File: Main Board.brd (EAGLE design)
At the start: 82.5 x 69.8 mm, 19 parts, among them U1 TPS61030RSAR

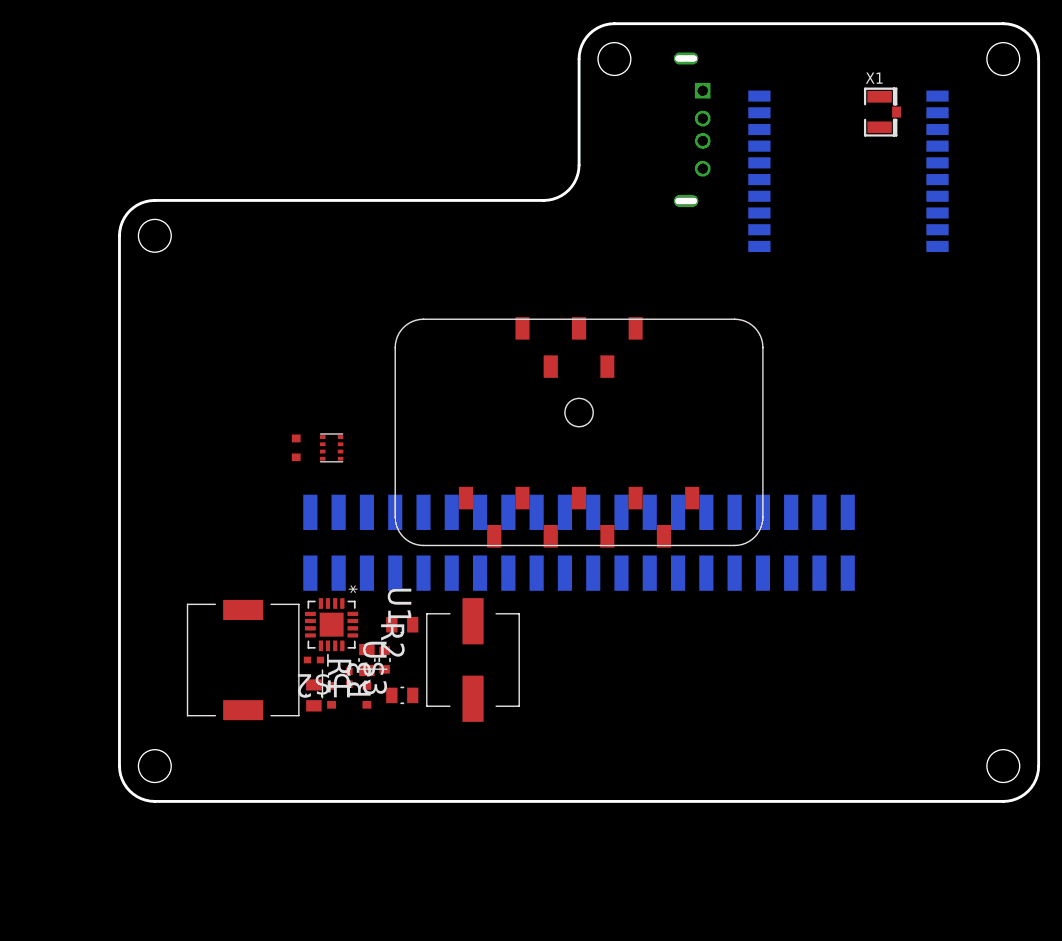
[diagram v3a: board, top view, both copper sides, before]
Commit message: Completed Motor Driver schematic
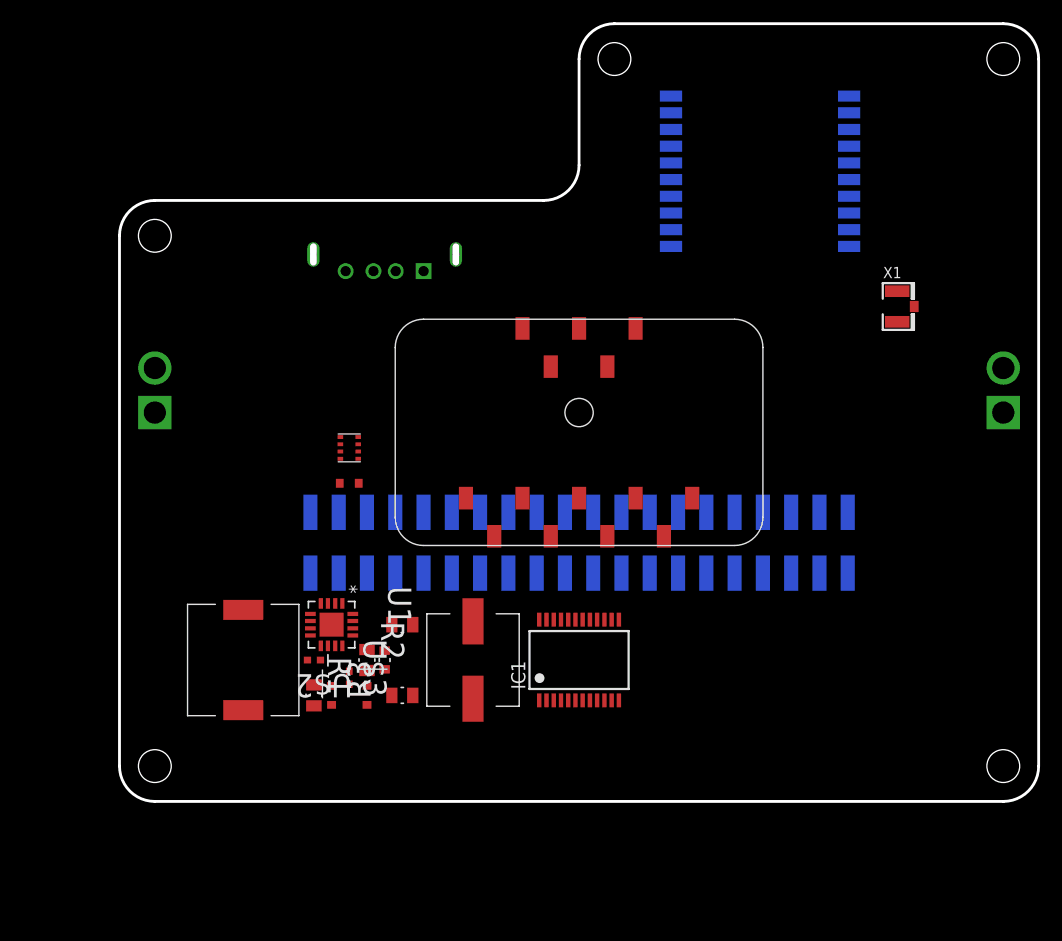
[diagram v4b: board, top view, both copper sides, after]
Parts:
- added IC1: TB6612FNG, Adafruit:SSOP24
- added U$15, U$16: MOTOR2, GoatFinder:BAT
- moved U$8 31.3 mm to (-17.5, 12.7), turned to 0 degrees
- moved X1 17.5 mm to (28.6, 9.53)
- moved U$5 7.94 mm to (15.9, 17.5)
- moved U$14 5.72 mm to (-20.6, -6.35), turned to 180 degrees
- moved U$13 1.59 mm to (-20.6, -3.17), turned to 0 degrees
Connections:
- new net +12V: IC1.13, IC1.14, IC1.24
- new net N$15: IC1.22, U$11.GPIO2
- new net N$16: IC1.1, IC1.2, U$15.P$1
- new net N$17: IC1.5, IC1.6, U$15.P$2
- new net N$18: IC1.7, IC1.8, U$16.P$1
- new net N$19: IC1.11, IC1.12, U$16.P$2
- new net N$20: IC1.21, U$11.GPIO3
- new net N$21: IC1.19, U$11.GPIO4
- new net N$22: IC1.17, U$11.GPIO5
- new net N$23: IC1.16, U$11.GPIO6
- new net PWMA: IC1.23, U$11.GPIO23
- new net PWMB: IC1.15, U$11.GPIO26
- net +3.3V: now also IC1.20
- net GND: now also IC1.10, IC1.18, IC1.3, IC1.4, IC1.9
- net N$10: now also U$11.SCL1; no longer U$11.SCL0
- net N$12: now also U$11.SDA1; no longer U$11.SDA0
- net N$13: now also U$11.SDA0; no longer U$11.SDA1
- net N$14: now also U$11.SCL0; no longer U$11.SCL1

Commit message: Modified part placment
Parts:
- moved U$3 29.5 mm to (-38.1, 0.00)
- moved R3 29.3 mm to (-36.5, 0.00)
- moved U$4 29.3 mm to (-38.1, -3.17)
- moved U$9 29.3 mm to (-34.9, -3.17)
- moved R1 29.2 mm to (-34.9, 1.59)
- moved R2 29.1 mm to (-33.3, 3.17)
- moved U$7 28.6 mm to (-31.8, 1.59)
- moved U$1 27.2 mm to (-33.3, 4.76), turned to 180 degrees
- moved U$12 26.3 mm to (-33.3, -11.1), turned to 180 degrees
- moved U$10 24.7 mm to (-33.3, -1.59)
- moved U$2 24.2 mm to (-33.3, 0.00)
- moved IC1 22.1 mm to (7.94, -1.59), flipped to the bottom, turned to 270 degrees
- moved U$5 19.4 mm to (0.00, 6.35)
- moved U$15 17.5 mm to (-20.6, 0.00), turned to 270 degrees
- moved U$16 17.5 mm to (20.6, 0.00), turned to 270 degrees
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
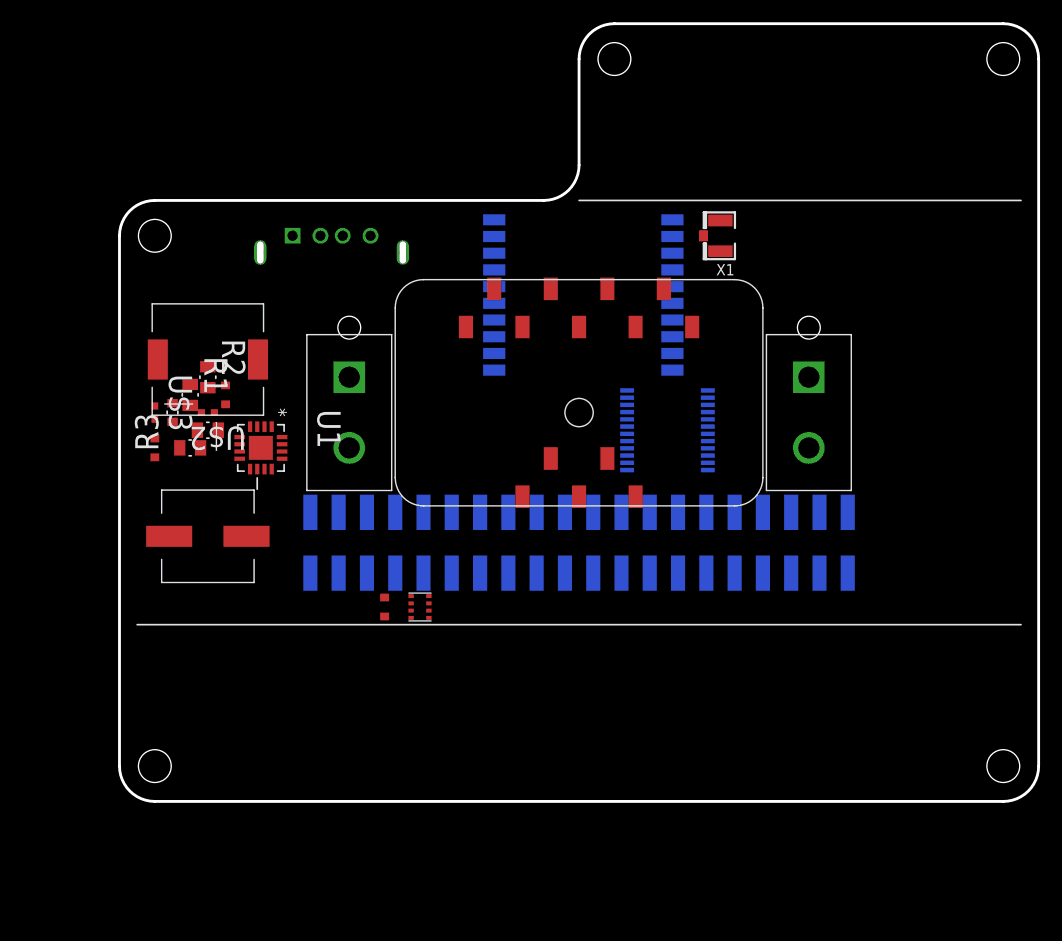
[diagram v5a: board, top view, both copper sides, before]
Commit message: Reduced Board Size and added Ground Planes
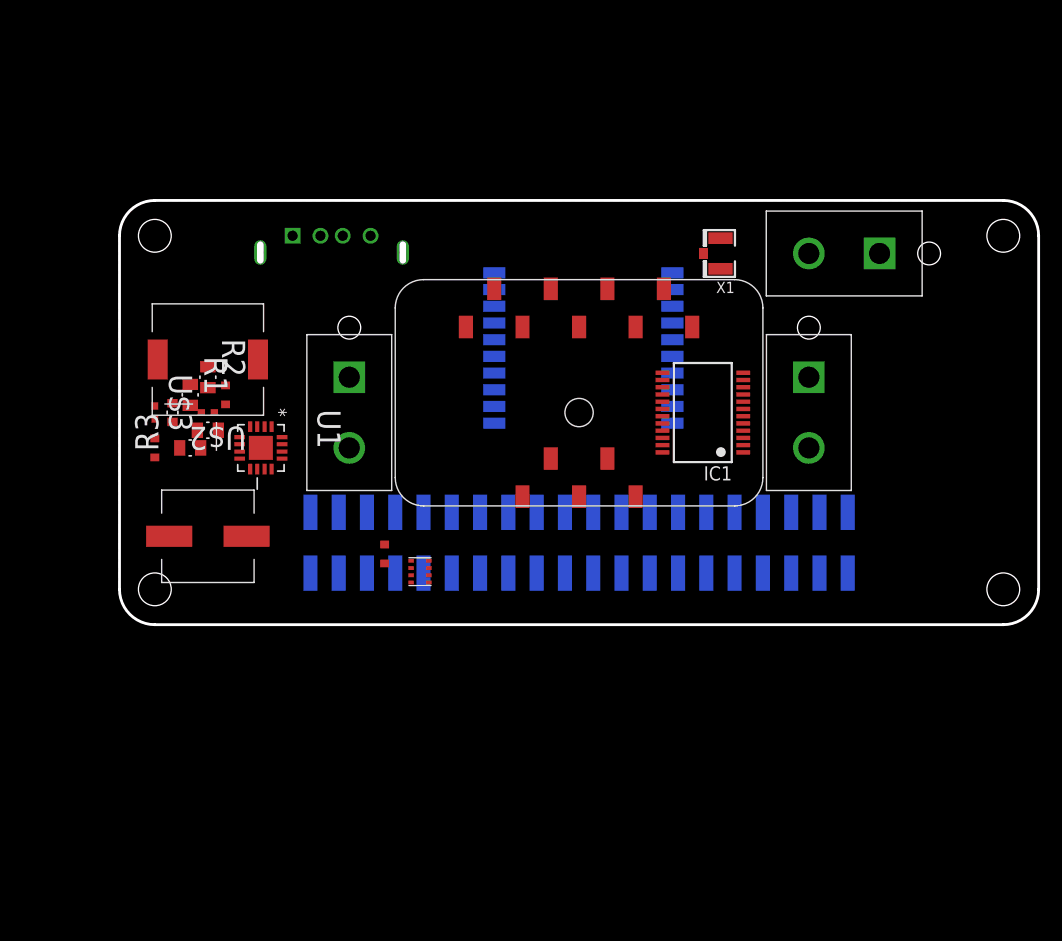
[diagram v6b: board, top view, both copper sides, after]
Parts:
- added U$17: MOTOR2, GoatFinder:BAT
- moved U$14 4.76 mm to (-17.5, -12.7)
- moved U$5 4.76 mm to (0.00, 1.59)
- moved IC1 3.55 mm to (11.1, 0.00), flipped to the top, turned to 90 degrees
- moved U$13 3.17 mm to (-14.3, -14.3)
- moved X1 1.59 mm to (12.7, 14.3)
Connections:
- removed net +12V: IC1.13, IC1.14, IC1.24
- net GND: now also U$17.P$2
- net VBAT: now also IC1.13, IC1.14, IC1.24, U$17.P$1
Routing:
- added copper zone on layer 1, net GND
- added copper zone on layer 16, net GND
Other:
- board size 82.5 x 69.8 mm -> 82.5 x 38.1 mm

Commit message: Components in place, beginning traces.
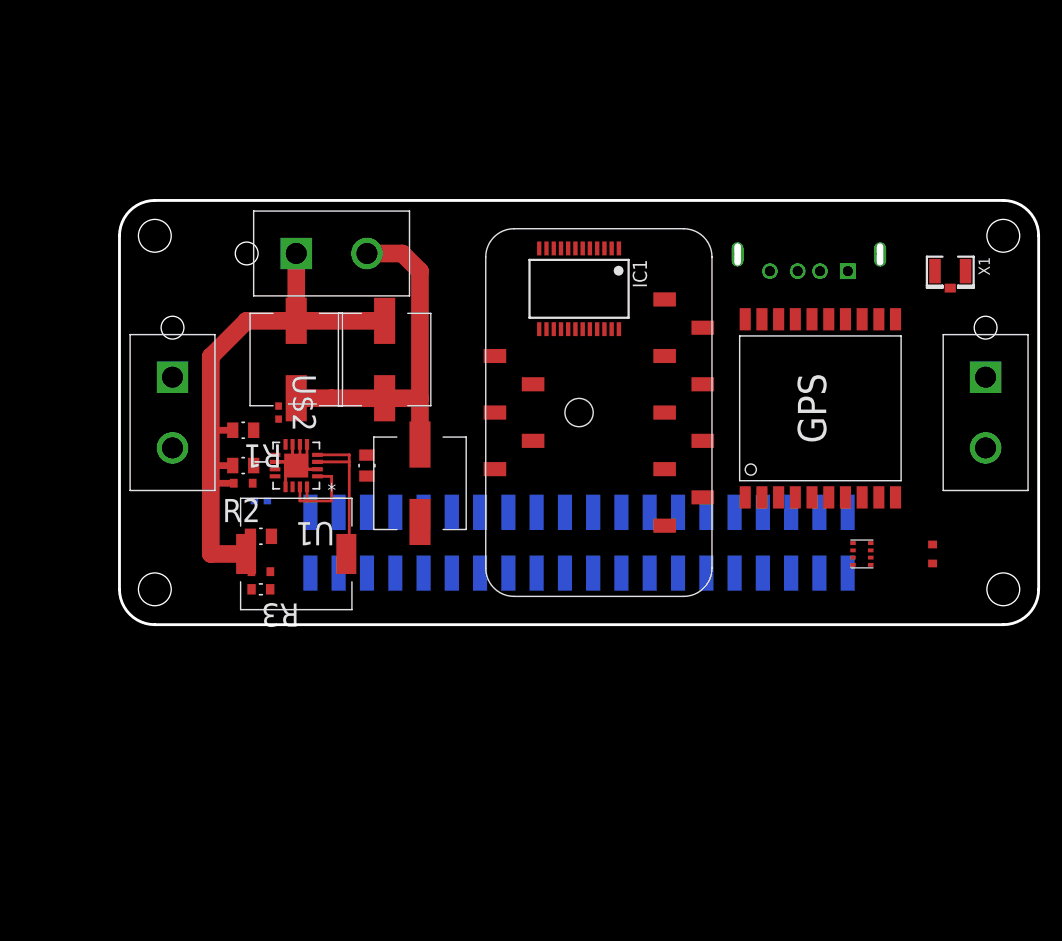
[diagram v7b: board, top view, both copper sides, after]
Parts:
- added U$18, U$19: 220, GoatFinder:220
- moved U$14 49.2 mm to (31.8, -12.7)
- moved U$17 46.0 mm to (-22.2, 14.3), turned to 0 degrees
- moved U$8 43.0 mm to (20.6, 12.7), turned to 0 degrees
- moved U$13 39.7 mm to (25.4, -12.7)
- moved X1 20.7 mm to (33.3, 12.7), turned to 270 degrees
- moved U$12 19.6 mm to (-14.3, -6.35), turned to 270 degrees
- moved U$1 19.2 mm to (-25.4, -12.7)
- moved R3 17.7 mm to (-28.6, -15.9), turned to 180 degrees
- moved U$5 17.5 mm to (17.5, 0.00), flipped to the top, turned to 90 degrees
- moved U$9 16.0 mm to (-19.1, -4.76), turned to 90 degrees
- moved U$15 15.9 mm to (-36.5, 0.00)
- moved U$16 15.9 mm to (36.5, 0.00)
- moved IC1 15.7 mm to (0.00, 11.1), turned to 180 degrees
- moved R2 15.1 mm to (-28.6, -11.1), turned to 0 degrees
- moved U$4 14.6 mm to (-28.6, -14.3), turned to 180 degrees
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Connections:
- net GND: now also U$18.P$2, U$19.P$2
- net VBAT: now also U$18.P$1, U$19.P$1
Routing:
- net GND: track 0.00 -> 51.7 mm
- net VBAT: track 0.00 -> 49.9 mm
- net N$2: track 0.00 -> 14.9 mm
- net +5V: track 0.00 -> 8.86 mm
- removed copper zone on layer 1, net GND
- removed copper zone on layer 16, net GND

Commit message: Added Ground Pours
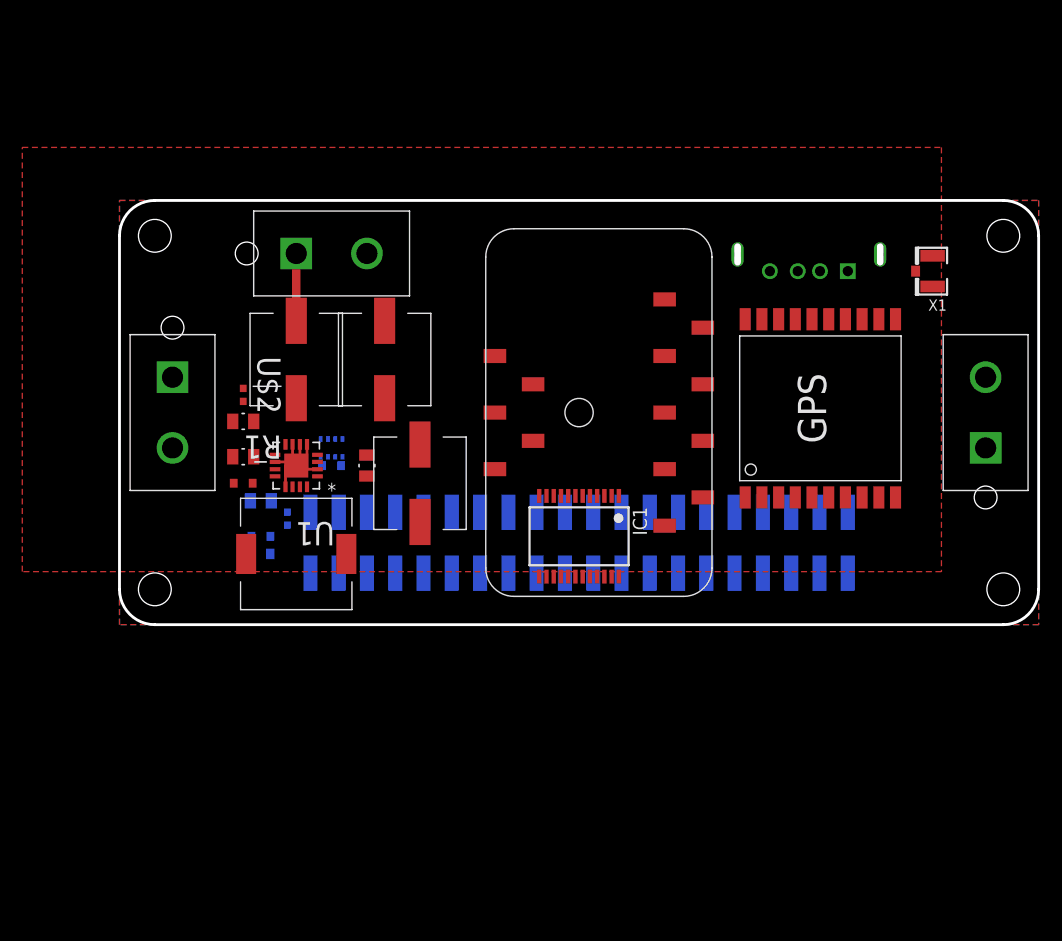
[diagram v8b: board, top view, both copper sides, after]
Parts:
- moved U$15 73.0 mm to (36.5, 0.00), turned to 90 degrees
- moved U$16 73.0 mm to (-36.5, 0.00)
- moved U$14 54.6 mm to (-22.2, -4.76), flipped to the bottom, turned to 180 degrees
- moved U$13 48.6 mm to (-22.2, -3.17), flipped to the bottom, turned to 270 degrees
- moved IC1 22.2 mm to (0.00, -11.1)
- moved U$2 3.55 mm to (-30.2, 1.59)
- moved R2 3.18 mm to (-28.6, -7.94), flipped to the bottom, turned to 180 degrees
- moved R3 3.18 mm to (-28.6, -12.7), flipped to the bottom, turned to 0 degrees
- moved U$4 3.17 mm to (-28.6, -11.1), flipped to the bottom, turned to 0 degrees
- moved U$3 2.86 mm to (-26.2, -9.53), turned to 90 degrees
- moved X1 1.59 mm to (31.8, 12.7), turned to 180 degrees
- moved U$10 0.79 mm to (-30.2, -3.97)
- moved R1 0.79 mm to (-30.2, -0.79)
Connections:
- removed net N$15: IC1.22, U$11.GPIO2
- removed net N$20: IC1.21, U$11.GPIO3
- removed net N$21: IC1.19, U$11.GPIO4
- removed net N$22: IC1.17, U$11.GPIO5
- removed net N$23: IC1.16, U$11.GPIO6
- removed net N$5: U$11.GPIO27, U$5.P$2
- removed net N$6: U$11.GPIO28, U$5.P$5
- removed net N$9: U$11.GPIO29, U$5.P$13
- new net GPIO0: U$11.GPIO0, U$5.P$13
- new net GPIO10: IC1.19, U$11.CE0
- new net GPIO11: IC1.22, U$11.CE1
- new net GPIO12: IC1.16, U$11.MOSI
- new net GPIO13: IC1.17, U$11.MISO
- new net GPIO14: IC1.21, U$11.SCLK
- new net GPIO4: U$11.GPIO4, U$5.P$5
- new net GPIO5: U$11.GPIO5, U$5.P$2
- new net MOTA: IC1.23
- new net MOTB: IC1.15
- net PWMA: no longer IC1.23
- net PWMB: no longer IC1.15
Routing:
- net VBAT: track 49.9 -> 6.05 mm
- net GND: track 51.7 -> 13.1 mm
- net N$2: track 14.9 -> 0.00 mm
- net +5V: track 8.86 -> 0.00 mm
- added copper zone on layer 1, net GND
- added copper zone on layer 16, net GND
